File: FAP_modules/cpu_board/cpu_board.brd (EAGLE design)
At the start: 100 x 60 mm, 35 parts, among them IC2 74HC245DW, IC3 74HC245DW, IC4 74HC04D, IC7 74HC245DW, IC8 74HC245DW, IC9 74HC245DW

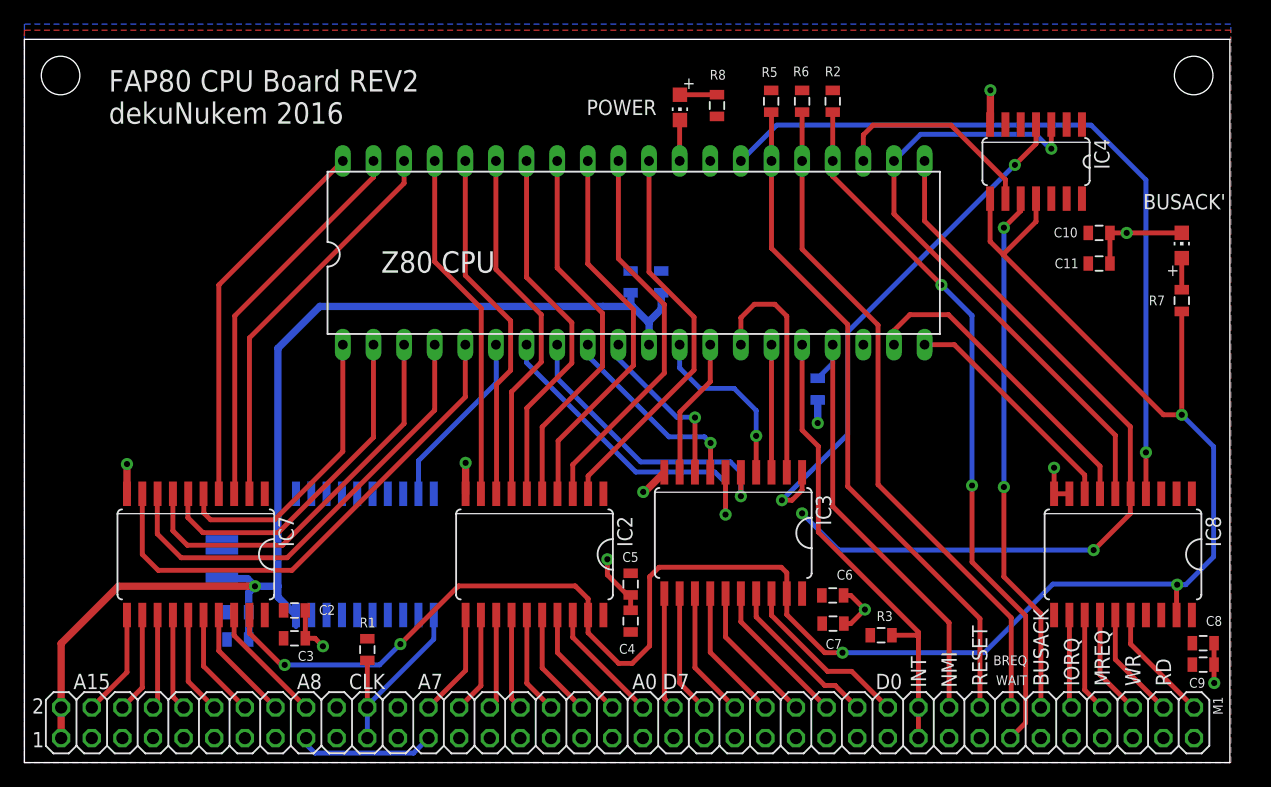
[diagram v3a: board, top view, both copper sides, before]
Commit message: added all Z80 signals on bus
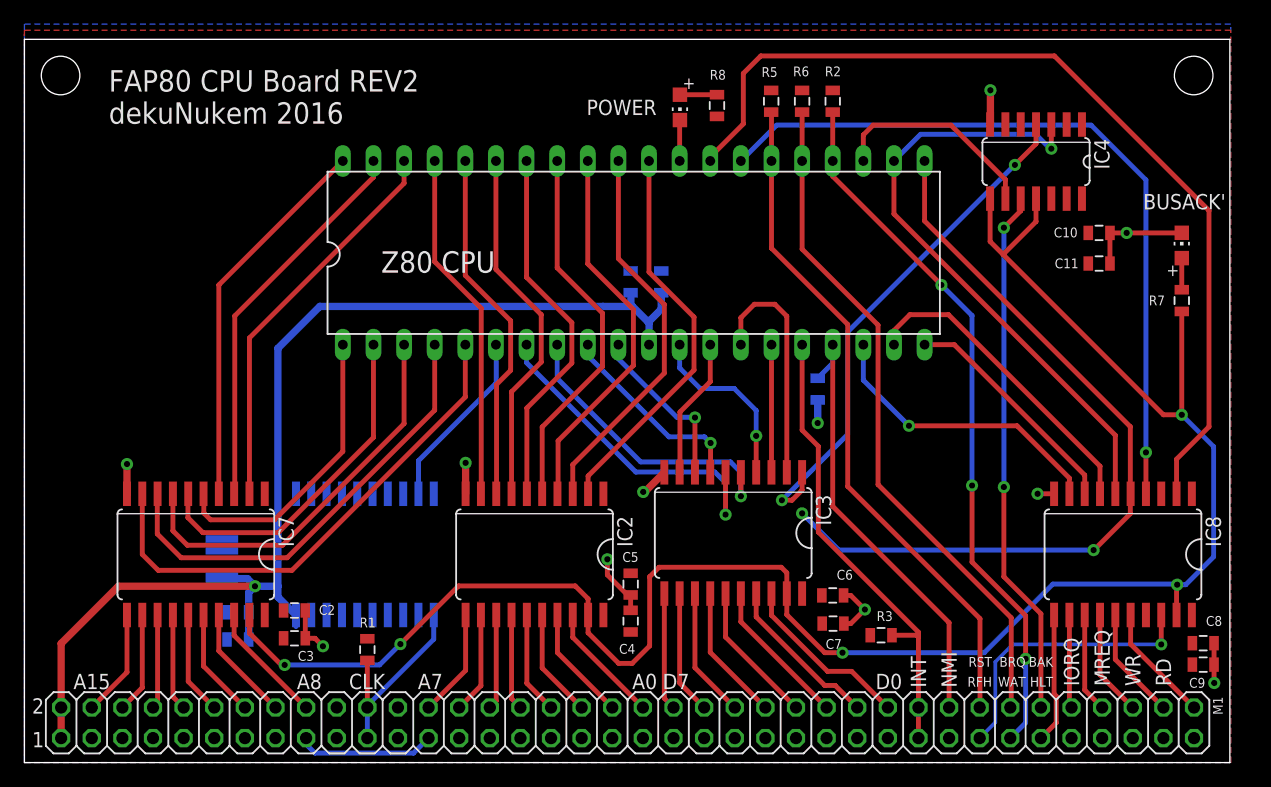
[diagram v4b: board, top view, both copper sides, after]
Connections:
- new net N$34: IC1.18, IC8.9
- new net N$37: IC8.11, U$1.HALT
- new net N$38: IC1.28, IC8.2
- new net N$70: IC8.18, U$1.REFRESH
- net +3V3: no longer IC8.2
- net GND: no longer IC8.9, U$1.GND@31, U$1.GND@33
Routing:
- net N$38: track 0.00 -> 77.6 mm
- net N$34: track 0.00 -> 24.7 mm, vias 0 -> 1
- net N$70: track 0.00 -> 23.7 mm, vias 0 -> 1
- net N$37: track 0.00 -> 10.8 mm
- net GND: track 54.2 -> 52.1 mm
- net N$32: vias 2 -> 3
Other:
- board text added: "BAK"
- board text added: "BRQ"
- board text added: "HLT"
- board text added: "RFH"
- board text added: "RST"
- board text added: "WAT"
- board text removed: "BREQ"
- board text removed: "BUSACK"
- board text removed: "RESET"
- board text removed: "WAIT"
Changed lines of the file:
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@@
 <text x="74.803" y="6.223" size="1.27" layer="25" rot="R90">INT</text>
 <text x="77.343" y="6.223" size="1.27" layer="25" rot="R90">NMI</text>
-<text x="79.883" y="6.35" size="1.27" layer="25" rot="R90">RESET</text>
-<text x="83.185" y="8.89" size="0.8128" layer="25" rot="R180">BREQ</text>
-<text x="84.963" y="6.35" size="1.27" layer="25" rot="R90">BUSACK</text>
+<text x="83.058" y="8.763" size="0.8128" layer="25" rot="R180">BRQ</text>
 <text x="87.503" y="6.35" size="1.27" layer="25" rot="R90">IORQ</text>
 <text x="90.043" y="6.35" size="1.27" layer="25" rot="R90">MREQ</text>
@@
 dekuNukem 2016</text>
 <text x="46.6344" y="53.721" size="1.27" layer="25">POWER</text>
-<text x="83.185" y="7.239" size="0.8128" layer="25" rot="R180">WAIT</text>
+<text x="83.058" y="7.112" size="0.8128" layer="25" rot="R180">WAT</text>
+<text x="80.264" y="7.112" size="0.8128" layer="25" rot="R180">RFH</text>
+<text x="80.264" y="8.763" size="0.8128" layer="25" rot="R180">RST</text>
+<text x="85.344" y="8.763" size="0.8128" layer="25" rot="R180">BAK</text>
+<text x="85.344" y="7.112" size="0.8128" layer="25" rot="R180">HLT</text>
 </plain>
 <attributes>
@@
 <contactref element="C11" pad="1"/>
 <contactref element="R8" pad="1"/>
-<contactref element="IC8" pad="2"/>
-<contactref element="IC8" pad="3"/>
 <contactref element="R1" pad="2"/>
 <contactref element="R2" pad="2"/>
@@
 <contactref element="IC4" pad="5"/>
 <contactref element="IC4" pad="13"/>
+<contactref element="IC8" pad="3"/>
 </signal>
 <signal name="+5V">
@@
 <contactref element="U$1" pad="GND@38"/>
 <contactref element="U$1" pad="GND@14"/>
-<contactref element="U$1" pad="GND@31"/>
 <contactref element="U$1" pad="GND@34"/>
 <contactref element="U$1" pad="GND@4"/>
@@
 <contactref element="U$1" pad="GND@37"/>
 <contactref element="U$1" pad="GND@16"/>
-<contactref element="U$1" pad="GND@33"/>
 <contactref element="U$1" pad="GND@19"/>
 <contactref element="U$1" pad="GND@3"/>
@@
 <via x="36.6014" y="24.8666" extent="1-16" drill="0.508"/>
 <via x="51.3334" y="22.4536" extent="1-16" drill="0.508"/>
-<via x="85.4202" y="24.4602" extent="1-16" drill="0.508"/>
+<via x="84.0486" y="22.3012" extent="1-16" drill="0.508"/>
 <wire x1="51.3334" y1="22.4536" x2="51.4604" y2="22.4536" width="0.4064" layer="1"/>
 <wire x1="51.4604" y1="22.4536" x2="53.086" y2="24.0792" width="0.6096" layer="1"/>
@@
 <wire x1="98.69" y1="6.6184" x2="98.69" y2="8.128" width="0.4064" layer="1"/>
 <wire x1="98.69" y1="8.128" x2="98.69" y2="9.906" width="0.4064" layer="1"/>
-<wire x1="85.4202" y1="24.4602" x2="85.4202" y2="22.3012" width="0.4064" layer="1"/>
+<wire x1="84.0486" y1="22.3012" x2="85.4202" y2="22.3012" width="0.4064" layer="1"/>
 <wire x1="91.44" y1="43.942" x2="90.054" y2="43.942" width="0.4064" layer="1"/>
 <wire x1="90.054" y1="43.942" x2="90.054" y2="41.402" width="0.4064" layer="1"/>
@@
 <wire x1="54.3814" y1="53.306" x2="54.356" y2="53.2806" width="0.4064" layer="1"/>
 <wire x1="54.356" y1="53.2806" x2="54.356" y2="49.911" width="0.4064" layer="1"/>
-<contactref element="IC8" pad="9"/>
-<wire x1="85.4202" y1="22.3012" x2="86.6902" y2="22.3012" width="0.4064" layer="1"/>
 <wire x1="50.292" y1="13.9082" x2="50.0236" y2="13.9082" width="0.4064" layer="1"/>
 <wire x1="50.0236" y1="13.9082" x2="48.3616" y2="15.5702" width="0.4064" layer="1"/>
@@
 </signal>
 <signal name="N$32">
-<contactref element="U$1" pad="WAIT"/>
 <contactref element="IC1" pad="24"/>
 <contactref element="R2" pad="1"/>
@@
 <wire x1="78.613" y1="22.987" x2="78.613" y2="16.637" width="0.4064" layer="1"/>
 <wire x1="78.613" y1="16.637" x2="83.058" y2="12.192" width="0.4064" layer="1"/>
-<wire x1="83.058" y1="12.192" x2="83.058" y2="3.302" width="0.4064" layer="1"/>
-<wire x1="83.058" y1="3.302" x2="81.788" y2="2.032" width="0.4064" layer="1"/>
+<contactref element="U$1" pad="WAIT"/>
+<wire x1="83.058" y1="12.192" x2="83.058" y2="8.6106" width="0.4064" layer="1"/>
+<via x="83.058" y="8.6106" extent="1-16" drill="0.5"/>
+<wire x1="83.058" y1="8.6106" x2="83.058" y2="3.302" width="0.4064" layer="16"/>
+<wire x1="83.058" y1="3.302" x2="81.788" y2="2.032" width="0.4064" layer="16"/>
+</signal>
+<signal name="N$34">
+<contactref element="IC1" pad="18"/>
+<contactref element="IC8" pad="9"/>
+<wire x1="69.596" y1="34.671" x2="69.596" y2="31.7246" width="0.4064" layer="16"/>
+<wire x1="69.596" y1="31.7246" x2="73.3806" y2="27.94" width="0.4064" layer="16"/>
+<via x="73.3806" y="27.94" extent="1-16" drill="0.5"/>
+<wire x1="73.3806" y1="27.94" x2="82.3468" y2="27.94" width="0.4064" layer="1"/>
+<wire x1="82.3468" y1="27.94" x2="86.6902" y2="23.5966" width="0.4064" layer="1"/>
+<wire x1="86.6902" y1="23.5966" x2="86.6902" y2="22.3012" width="0.4064" layer="1"/>
+</signal>
+<signal name="N$37">
+<contactref element="IC8" pad="11"/>
+<contactref element="U$1" pad="HALT"/>
+<wire x1="85.4202" y1="12.2428" x2="85.4202" y2="5.6896" width="0.4064" layer="1"/>
+<wire x1="85.4202" y1="5.6896" x2="85.598" y2="5.5118" width="0.4064" layer="1"/>
+<wire x1="85.598" y1="5.5118" x2="85.598" y2="3.302" width="0.4064" layer="1"/>
+<wire x1="85.598" y1="3.302" x2="84.328" y2="2.032" width="0.4064" layer="1"/>
+</signal>
+<signal name="N$38">
+<contactref element="IC1" pad="28"/>
+<contactref element="IC8" pad="2"/>
+<wire x1="56.896" y1="49.911" x2="56.896" y2="50.2412" width="0.4064" layer="1"/>
+<wire x1="56.896" y1="50.2412" x2="59.6392" y2="52.9844" width="0.4064" layer="1"/>
+<wire x1="59.6392" y1="52.9844" x2="59.6392" y2="57.1754" width="0.4064" layer="1"/>
+<wire x1="98.2726" y1="45.7962" x2="98.2726" y2="27.8638" width="0.4064" layer="1"/>
+<wire x1="98.2726" y1="27.8638" x2="95.5802" y2="25.1714" width="0.4064" layer="1"/>
+<wire x1="95.5802" y1="25.1714" x2="95.5802" y2="22.3012" width="0.4064" layer="1"/>
+<wire x1="59.6392" y1="57.1754" x2="61.087" y2="58.6232" width="0.4064" layer="1"/>
+<wire x1="61.087" y1="58.6232" x2="85.4456" y2="58.6232" width="0.4064" layer="1"/>
+<wire x1="85.4456" y1="58.6232" x2="98.2726" y2="45.7962" width="0.4064" layer="1"/>
+</signal>
+<signal name="N$70">
+<contactref element="IC8" pad="18"/>
+<contactref element="U$1" pad="REFRESH"/>
+<wire x1="94.3102" y1="12.2428" x2="94.3102" y2="9.8044" width="0.4064" layer="1"/>
+<via x="94.3102" y="9.8044" extent="1-16" drill="0.5"/>
+<wire x1="94.3102" y1="9.8044" x2="81.9912" y2="9.8044" width="0.3048" layer="16"/>
+<wire x1="81.9912" y1="9.8044" x2="80.5434" y2="8.3566" width="0.3048" layer="16"/>
+<wire x1="80.5434" y1="8.3566" x2="80.5434" y2="3.3274" width="0.3048" layer="16"/>
+<wire x1="80.5434" y1="3.3274" x2="79.248" y2="2.032" width="0.3048" layer="16"/>
 </signal>
 </signals>

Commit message: board cleanup
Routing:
- net N$32: vias 3 -> 2
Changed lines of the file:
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@@
 </class>
 </classes>
-<designrules name="SparkFun-2-layer-STANDARD">
+<designrules name="SparkFun-2-layer-TIGHT">
 <description language="en">&lt;b&gt;SparkFun 2 Layer Design Rule Checks - STANDARD/TIGHT/FAB-LIMIT&lt;/b&gt;
 &lt;p&gt;
@@
 <param name="mtCopper" value="0.035mm 0.035mm 0.035mm 0.035mm 0.035mm 0.035mm 0.035mm 0.035mm 0.035mm 0.035mm 0.035mm 0.035mm 0.035mm 0.035mm 0.035mm 0.035mm"/>
 <param name="mtIsolate" value="1.5mm 0.15mm 0.2mm 0.15mm 0.2mm 0.15mm 0.2mm 0.15mm 0.2mm 0.15mm 0.2mm 0.15mm 0.2mm 0.15mm 0.2mm"/>
-<param name="mdWireWire" value="10mil"/>
-<param name="mdWirePad" value="8mil"/>
-<param name="mdWireVia" value="10mil"/>
-<param name="mdPadPad" value="8mil"/>
-<param name="mdPadVia" value="10mil"/>
-<param name="mdViaVia" value="10mil"/>
-<param name="mdSmdPad" value="8mil"/>
-<param name="mdSmdVia" value="8mil"/>
-<param name="mdSmdSmd" value="8mil"/>
+<param name="mdWireWire" value="7mil"/>
+<param name="mdWirePad" value="7mil"/>
+<param name="mdWireVia" value="7mil"/>
+<param name="mdPadPad" value="7mil"/>
+<param name="mdPadVia" value="7mil"/>
+<param name="mdViaVia" value="7mil"/>
+<param name="mdSmdPad" value="7mil"/>
+<param name="mdSmdVia" value="7mil"/>
+<param name="mdSmdSmd" value="7mil"/>
 <param name="mdViaViaSameLayer" value="8mil"/>
 <param name="mnLayersViaInSmd" value="2"/>
-<param name="mdCopperDimension" value="8mil"/>
-<param name="mdDrill" value="8mil"/>
+<param name="mdCopperDimension" value="7mil"/>
+<param name="mdDrill" value="7mil"/>
 <param name="mdSmdStop" value="0mil"/>
-<param name="msWidth" value="10mil"/>
-<param name="msDrill" value="20mil"/>
+<param name="msWidth" value="7mil"/>
+<param name="msDrill" value="15mil"/>
 <param name="msMicroVia" value="9.99mm"/>
 <param name="msBlindViaRatio" value="0.5"/>
@@
 <param name="rvMicroViaOuter" value="0.25"/>
 <param name="rvMicroViaInner" value="0.25"/>
-<param name="rlMinPadTop" value="10mil"/>
+<param name="rlMinPadTop" value="7mil"/>
 <param name="rlMaxPadTop" value="20mil"/>
-<param name="rlMinPadInner" value="10mil"/>
+<param name="rlMinPadInner" value="7mil"/>
 <param name="rlMaxPadInner" value="20mil"/>
-<param name="rlMinPadBottom" value="10mil"/>
+<param name="rlMinPadBottom" value="7mil"/>
 <param name="rlMaxPadBottom" value="20mil"/>
-<param name="rlMinViaOuter" value="10mil"/>
+<param name="rlMinViaOuter" value="7mil"/>
 <param name="rlMaxViaOuter" value="20mil"/>
-<param name="rlMinViaInner" value="10mil"/>
+<param name="rlMinViaInner" value="7mil"/>
 <param name="rlMaxViaInner" value="20mil"/>
 <param name="rlMinMicroViaOuter" value="4mil"/>
@@
 <wire x1="78.613" y1="16.637" x2="83.058" y2="12.192" width="0.4064" layer="1"/>
 <contactref element="U$1" pad="WAIT"/>
-<wire x1="83.058" y1="12.192" x2="83.058" y2="8.6106" width="0.4064" layer="1"/>
-<via x="83.058" y="8.6106" extent="1-16" drill="0.5"/>
-<wire x1="83.058" y1="8.6106" x2="83.058" y2="3.302" width="0.4064" layer="16"/>
-<wire x1="83.058" y1="3.302" x2="81.788" y2="2.032" width="0.4064" layer="16"/>
+<wire x1="83.058" y1="12.192" x2="83.058" y2="3.302" width="0.4064" layer="1"/>
+<wire x1="83.058" y1="3.302" x2="81.788" y2="2.032" width="0.4064" layer="1"/>
 </signal>
 <signal name="N$34">

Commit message: board cleanup
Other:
- board text added: "FAP80 CPU Board V2 dekuNukem 2016"
- board text removed: "FAP80 CPU Board REV2 dekuNukem 2016"
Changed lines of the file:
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@@
 <text x="0.635" y="4.064" size="1.27" layer="25">2</text>
 <text x="92.8116" y="45.8978" size="1.27" layer="25">BUSACK'</text>
-<text x="7" y="53" size="1.778" layer="25">FAP80 CPU Board REV2
+<text x="7" y="53" size="1.778" layer="25">FAP80 CPU Board V2
 dekuNukem 2016</text>
 <text x="46.6344" y="53.721" size="1.27" layer="25">POWER</text>
